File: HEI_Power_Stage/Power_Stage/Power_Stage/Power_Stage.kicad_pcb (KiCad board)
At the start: 6 copper layers, 119.6 x 65.3 mm, 152 parts, among them IC1 ACS730KLCTR-65ABT, IC2 ACS730KLCTR-65ABT, IC3 ACS730KLCTR-65ABT, IC4 AMC1311DWVR, IC9 ACS730KLCTR-65ABT, J1 Screw_Terminal_01x01, J2 Screw_Terminal_01x01, J3 Screw_Terminal_01x01, J4 Screw_Terminal_01x01, J5 Screw_Terminal_01x01, J8 Conn_02x07_Odd_Even, J9 Conn_02x07_Odd_Even, Q1 EPC2304ENGRT, Q2 EPC2304ENGRT, Q3 EPC2304ENGRT, Q4 EPC2304ENGRT, Q5 EPC2304ENGRT, Q6 EPC2304ENGRT, U2 MP18831-4AGY, U3 MP18831-4AGY, U5 MP18831-4AGY

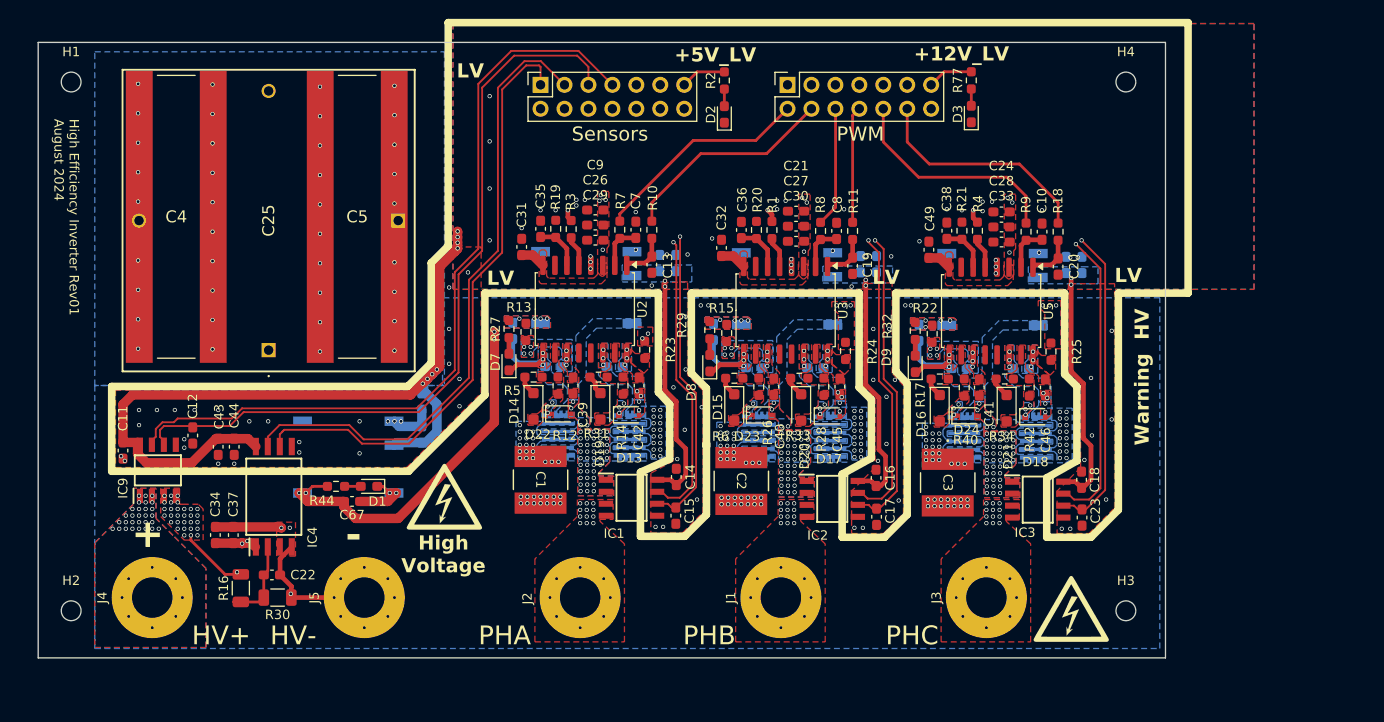
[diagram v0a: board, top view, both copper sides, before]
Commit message: allegro gate driver version schematic overhall and layout
layout and routing almost complete for allegro gate drivers
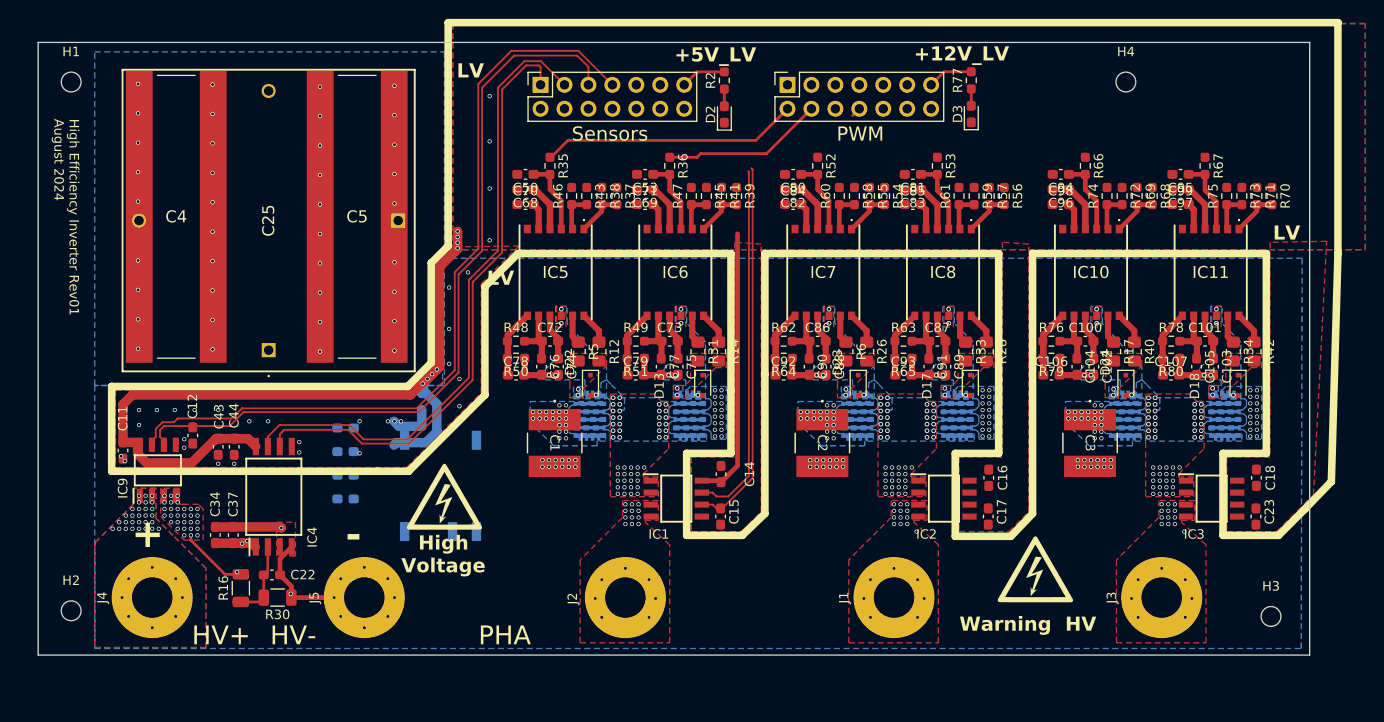
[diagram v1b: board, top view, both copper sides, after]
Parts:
- removed C13, C19, C20: 470pF, Capacitor_SMD:C_0603_1608Metric_Pad1.08x0.95mm_HandSolder
- removed C21, C24: 10uF, Capacitor_SMD:C_0603_1608Metric_Pad1.08x0.95mm_HandSolder
- removed C26, C27, C28, C39, C40, C41, C42, C45, C46, C59, C60, C61, C66: 1uF, Capacitor_SMD:C_0603_1608Metric_Pad1.08x0.95mm_HandSolder
- removed C29, C30, C31, C32, C33, C47, C48, C49, C51, C52, C54, C55: 0.1uF, Capacitor_SMD:C_0603_1608Metric_Pad1.08x0.95mm_HandSolder
- removed C35, C36, C38: 2.2nF, Capacitor_SMD:C_0603_1608Metric_Pad1.08x0.95mm_HandSolder
- removed C56, C57, C58, C62, C63, C64, C65, C67: 4.7uF, Capacitor_SMD:C_0603_1608Metric_Pad1.08x0.95mm_HandSolder
- removed D1, D7, D8, D9: G, LED_SMD:LED_0603_1608Metric_Pad1.05x0.95mm_HandSolder
- removed D14, D15, D16, D19, D20, D21: 300mV 1A, Diode_SMD:D_SOD-123F
- removed PS2, PS3, PS4: CRE1S0505MC, CRE1S0505MC_KiCad:CRE1S0505MC
- removed R1, R10, R11, R13, R15, R18, R22, R23, R24, R25, R3, R4, R7, R8, R9: 0, Resistor_SMD:R_0603_1608Metric_Pad0.98x0.95mm_HandSolder
- removed R19, R20, R21: 10k, Resistor_SMD:R_0603_1608Metric_Pad0.98x0.95mm_HandSolder
- removed R27, R29, R32, R44: 440, Resistor_SMD:R_0603_1608Metric_Pad0.98x0.95mm_HandSolder
- removed U2, U3, U5: MP18831-4AGY, Package_SO:SOIC-16W_7.5x10.3mm_P1.27mm
- added C100: 100nF, Capacitor_SMD:C_0603_1608Metric_Pad1.08x0.95mm_HandSolder, F.Cu at (210.1, 72.7)
- added C101: 100nF, Capacitor_SMD:C_0603_1608Metric_Pad1.08x0.95mm_HandSolder, F.Cu at (222.8, 72.7)
- added C102: 100nF, Capacitor_SMD:C_0603_1608Metric_Pad1.08x0.95mm_HandSolder, F.Cu at (211.0, 75.4)
- added C103: 100nF, Capacitor_SMD:C_0603_1608Metric_Pad1.08x0.95mm_HandSolder, F.Cu at (223.7, 75.4)
- added C104: 100nF, Capacitor_SMD:C_0603_1608Metric_Pad1.08x0.95mm_HandSolder, F.Cu at (209.2, 75.4)
- added C105: 100nF, Capacitor_SMD:C_0603_1608Metric_Pad1.08x0.95mm_HandSolder, F.Cu at (221.9, 75.4)
- added C106: 100pF, Capacitor_SMD:C_0603_1608Metric_Pad1.08x0.95mm_HandSolder, F.Cu at (206.5, 76.3)
- added C107: 100pF, Capacitor_SMD:C_0603_1608Metric_Pad1.08x0.95mm_HandSolder, F.Cu at (219.2, 76.3)
- added C50: 75pF, Capacitor_SMD:C_0603_1608Metric_Pad1.08x0.95mm_HandSolder, F.Cu at (150.7, 55.0)
- added C53: 75pF, Capacitor_SMD:C_0603_1608Metric_Pad1.08x0.95mm_HandSolder, F.Cu at (163.4, 55.0)
- added C68: 1uF, Capacitor_SMD:C_0603_1608Metric_Pad1.08x0.95mm_HandSolder, F.Cu at (150.7, 56.6)
- added C69: 1uF, Capacitor_SMD:C_0603_1608Metric_Pad1.08x0.95mm_HandSolder, F.Cu at (163.4, 56.6)
- added C70: 1uF, Capacitor_SMD:C_0603_1608Metric_Pad1.08x0.95mm_HandSolder, F.Cu at (150.7, 58.2)
- added C71: 1uF, Capacitor_SMD:C_0603_1608Metric_Pad1.08x0.95mm_HandSolder, F.Cu at (163.4, 58.2)
- added C72: 100nF, Capacitor_SMD:C_0603_1608Metric_Pad1.08x0.95mm_HandSolder, F.Cu at (153.3, 72.7)
- added C73: 100nF, Capacitor_SMD:C_0603_1608Metric_Pad1.08x0.95mm_HandSolder, F.Cu at (166.0, 72.7)
- added C74: 100nF, Capacitor_SMD:C_0603_1608Metric_Pad1.08x0.95mm_HandSolder, F.Cu at (154.2, 75.4)
- added C75: 100nF, Capacitor_SMD:C_0603_1608Metric_Pad1.08x0.95mm_HandSolder, F.Cu at (166.9, 75.4)
- added C76: 100nF, Capacitor_SMD:C_0603_1608Metric_Pad1.08x0.95mm_HandSolder, F.Cu at (152.4, 75.4)
- added C77: 100nF, Capacitor_SMD:C_0603_1608Metric_Pad1.08x0.95mm_HandSolder, F.Cu at (165.1, 75.4)
- added C78: 100pF, Capacitor_SMD:C_0603_1608Metric_Pad1.08x0.95mm_HandSolder, F.Cu at (149.7, 76.3)
- added C79: 100pF, Capacitor_SMD:C_0603_1608Metric_Pad1.08x0.95mm_HandSolder, F.Cu at (162.4, 76.3)
- added C80: 75pF, Capacitor_SMD:C_0603_1608Metric_Pad1.08x0.95mm_HandSolder, F.Cu at (179.1, 55.0)
- added C81: 75pF, Capacitor_SMD:C_0603_1608Metric_Pad1.08x0.95mm_HandSolder, F.Cu at (191.8, 55.0)
- added C82: 1uF, Capacitor_SMD:C_0603_1608Metric_Pad1.08x0.95mm_HandSolder, F.Cu at (179.1, 56.6)
- added C83: 1uF, Capacitor_SMD:C_0603_1608Metric_Pad1.08x0.95mm_HandSolder, F.Cu at (191.8, 56.6)
- added C84: 1uF, Capacitor_SMD:C_0603_1608Metric_Pad1.08x0.95mm_HandSolder, F.Cu at (179.1, 58.2)
- added C85: 1uF, Capacitor_SMD:C_0603_1608Metric_Pad1.08x0.95mm_HandSolder, F.Cu at (191.8, 58.2)
- added C86: 100nF, Capacitor_SMD:C_0603_1608Metric_Pad1.08x0.95mm_HandSolder, F.Cu at (181.7, 72.7)
- added C87: 100nF, Capacitor_SMD:C_0603_1608Metric_Pad1.08x0.95mm_HandSolder, F.Cu at (194.4, 72.7)
- added C88: 100nF, Capacitor_SMD:C_0603_1608Metric_Pad1.08x0.95mm_HandSolder, F.Cu at (182.6, 75.4)
- added C89: 100nF, Capacitor_SMD:C_0603_1608Metric_Pad1.08x0.95mm_HandSolder, F.Cu at (195.3, 75.4)
- added C90: 100nF, Capacitor_SMD:C_0603_1608Metric_Pad1.08x0.95mm_HandSolder, F.Cu at (180.8, 75.4)
- added C91: 100nF, Capacitor_SMD:C_0603_1608Metric_Pad1.08x0.95mm_HandSolder, F.Cu at (193.5, 75.4)
- added C92: 100pF, Capacitor_SMD:C_0603_1608Metric_Pad1.08x0.95mm_HandSolder, F.Cu at (178.1, 76.3)
- added C93: 100pF, Capacitor_SMD:C_0603_1608Metric_Pad1.08x0.95mm_HandSolder, F.Cu at (190.8, 76.3)
- added C94: 75pF, Capacitor_SMD:C_0603_1608Metric_Pad1.08x0.95mm_HandSolder, F.Cu at (207.5, 55.0)
- added C95: 75pF, Capacitor_SMD:C_0603_1608Metric_Pad1.08x0.95mm_HandSolder, F.Cu at (220.2, 55.0)
- added C96: 1uF, Capacitor_SMD:C_0603_1608Metric_Pad1.08x0.95mm_HandSolder, F.Cu at (207.5, 56.6)
- added C97: 1uF, Capacitor_SMD:C_0603_1608Metric_Pad1.08x0.95mm_HandSolder, F.Cu at (220.2, 56.6)
- added C98: 1uF, Capacitor_SMD:C_0603_1608Metric_Pad1.08x0.95mm_HandSolder, F.Cu at (207.5, 58.2)
- added C99: 1uF, Capacitor_SMD:C_0603_1608Metric_Pad1.08x0.95mm_HandSolder, F.Cu at (220.2, 58.2)
- added IC10: AHV85111KNHTR, AHV85111_KiCad:AHV85111KNHTR, F.Cu at (210.7, 65.4)
- added IC11: AHV85111KNHTR, AHV85111_KiCad:AHV85111KNHTR, F.Cu at (223.4, 65.4)
- added IC5: AHV85111KNHTR, AHV85111_KiCad:AHV85111KNHTR, F.Cu at (153.9, 65.4)
- added IC6: AHV85111KNHTR, AHV85111_KiCad:AHV85111KNHTR, F.Cu at (166.6, 65.4)
- added IC7: AHV85111KNHTR, AHV85111_KiCad:AHV85111KNHTR, F.Cu at (182.3, 65.4)
- added IC8: AHV85111KNHTR, AHV85111_KiCad:AHV85111KNHTR, F.Cu at (195.0, 65.4)
- added R35: 0, Resistor_SMD:R_0603_1608Metric_Pad0.98x0.95mm_HandSolder, F.Cu at (153.3, 54.1)
- added R36: 0, Resistor_SMD:R_0603_1608Metric_Pad0.98x0.95mm_HandSolder, F.Cu at (166.0, 54.1)
- added R37: 0, Resistor_SMD:R_0603_1608Metric_Pad0.98x0.95mm_HandSolder, F.Cu at (160.4, 57.3)
- added R38: 0, Resistor_SMD:R_0603_1608Metric_Pad0.98x0.95mm_HandSolder, F.Cu at (158.8, 57.3)
- added R39: 0, Resistor_SMD:R_0603_1608Metric_Pad0.98x0.95mm_HandSolder, F.Cu at (173.1, 57.3)
- added R41: 0, Resistor_SMD:R_0603_1608Metric_Pad0.98x0.95mm_HandSolder, F.Cu at (171.5, 57.3)
- added R43: 100k, Resistor_SMD:R_0603_1608Metric_Pad0.98x0.95mm_HandSolder, F.Cu at (157.2, 57.3)
- added R45: 100k, Resistor_SMD:R_0603_1608Metric_Pad0.98x0.95mm_HandSolder, F.Cu at (169.9, 57.3)
- added R46: 0, Resistor_SMD:R_0603_1608Metric_Pad0.98x0.95mm_HandSolder, F.Cu at (155.6, 57.3)
- added R47: 0, Resistor_SMD:R_0603_1608Metric_Pad0.98x0.95mm_HandSolder, F.Cu at (168.3, 57.3)
- added R48: 32.4k, Resistor_SMD:R_0603_1608Metric_Pad0.98x0.95mm_HandSolder, F.Cu at (149.7, 72.7)
- added R49: 32.4k, Resistor_SMD:R_0603_1608Metric_Pad0.98x0.95mm_HandSolder, F.Cu at (162.4, 72.7)
- added R50: 100k, Resistor_SMD:R_0603_1608Metric_Pad0.98x0.95mm_HandSolder, F.Cu at (149.7, 74.5)
- added R51: 100k, Resistor_SMD:R_0603_1608Metric_Pad0.98x0.95mm_HandSolder, F.Cu at (162.4, 74.5)
- added R52: 0, Resistor_SMD:R_0603_1608Metric_Pad0.98x0.95mm_HandSolder, F.Cu at (181.7, 54.1)
- added R53: 0, Resistor_SMD:R_0603_1608Metric_Pad0.98x0.95mm_HandSolder, F.Cu at (194.4, 54.1)
- added R54: 0, Resistor_SMD:R_0603_1608Metric_Pad0.98x0.95mm_HandSolder, F.Cu at (188.8, 57.3)
- added R55: 0, Resistor_SMD:R_0603_1608Metric_Pad0.98x0.95mm_HandSolder, F.Cu at (187.2, 57.3)
- added R56: 0, Resistor_SMD:R_0603_1608Metric_Pad0.98x0.95mm_HandSolder, F.Cu at (201.5, 57.3)
- added R57: 0, Resistor_SMD:R_0603_1608Metric_Pad0.98x0.95mm_HandSolder, F.Cu at (199.9, 57.3)
- added R58: 100k, Resistor_SMD:R_0603_1608Metric_Pad0.98x0.95mm_HandSolder, F.Cu at (185.6, 57.3)
- added R59: 100k, Resistor_SMD:R_0603_1608Metric_Pad0.98x0.95mm_HandSolder, F.Cu at (198.3, 57.3)
- added R60: 0, Resistor_SMD:R_0603_1608Metric_Pad0.98x0.95mm_HandSolder, F.Cu at (184.0, 57.3)
- added R61: 0, Resistor_SMD:R_0603_1608Metric_Pad0.98x0.95mm_HandSolder, F.Cu at (196.7, 57.3)
- added R62: 32.4k, Resistor_SMD:R_0603_1608Metric_Pad0.98x0.95mm_HandSolder, F.Cu at (178.1, 72.7)
- added R63: 32.4k, Resistor_SMD:R_0603_1608Metric_Pad0.98x0.95mm_HandSolder, F.Cu at (190.8, 72.7)
- added R64: 100k, Resistor_SMD:R_0603_1608Metric_Pad0.98x0.95mm_HandSolder, F.Cu at (178.1, 74.5)
- added R65: 100k, Resistor_SMD:R_0603_1608Metric_Pad0.98x0.95mm_HandSolder, F.Cu at (190.8, 74.5)
- added R66: 0, Resistor_SMD:R_0603_1608Metric_Pad0.98x0.95mm_HandSolder, F.Cu at (210.1, 54.1)
- added R67: 0, Resistor_SMD:R_0603_1608Metric_Pad0.98x0.95mm_HandSolder, F.Cu at (222.8, 54.1)
- added R68: 0, Resistor_SMD:R_0603_1608Metric_Pad0.98x0.95mm_HandSolder, F.Cu at (217.2, 57.3)
- added R69: 0, Resistor_SMD:R_0603_1608Metric_Pad0.98x0.95mm_HandSolder, F.Cu at (215.6, 57.3)
- added R70: 0, Resistor_SMD:R_0603_1608Metric_Pad0.98x0.95mm_HandSolder, F.Cu at (229.9, 57.3)
- added R71: 0, Resistor_SMD:R_0603_1608Metric_Pad0.98x0.95mm_HandSolder, F.Cu at (228.3, 57.3)
- added R72: 100k, Resistor_SMD:R_0603_1608Metric_Pad0.98x0.95mm_HandSolder, F.Cu at (214.0, 57.3)
- added R73: 100k, Resistor_SMD:R_0603_1608Metric_Pad0.98x0.95mm_HandSolder, F.Cu at (226.7, 57.3)
- added R74: 0, Resistor_SMD:R_0603_1608Metric_Pad0.98x0.95mm_HandSolder, F.Cu at (212.4, 57.3)
- added R75: 0, Resistor_SMD:R_0603_1608Metric_Pad0.98x0.95mm_HandSolder, F.Cu at (225.1, 57.3)
- added R76: 32.4k, Resistor_SMD:R_0603_1608Metric_Pad0.98x0.95mm_HandSolder, F.Cu at (206.5, 72.7)
- added R78: 32.4k, Resistor_SMD:R_0603_1608Metric_Pad0.98x0.95mm_HandSolder, F.Cu at (219.2, 72.7)
- added R79: 100k, Resistor_SMD:R_0603_1608Metric_Pad0.98x0.95mm_HandSolder, F.Cu at (206.5, 74.5)
- added R80: 100k, Resistor_SMD:R_0603_1608Metric_Pad0.98x0.95mm_HandSolder, F.Cu at (219.2, 74.5)
- C10, C8: value 470pF -> 2.2uF; moved to B.Cu
- C7: value 470pF -> 1uF; moved to B.Cu
- C9: value 10uF -> 1uF; moved to B.Cu
- R12, R14, R26, R28, R40, R42: footprint Resistor_SMD:R_0603_1608Metric_Pad0.98x0.95mm_HandSolder -> Resistor_SMD:R_0805_2012Metric_Pad1.20x1.40mm_HandSolder
- R17, R31, R33, R34, R5, R6: value 0 -> 0.5; footprint Resistor_SMD:R_0603_1608Metric_Pad0.98x0.95mm_HandSolder -> Resistor_SMD:R_0805_2012Metric_Pad1.20x1.40mm_HandSolder
- moved C10 79.1 mm to (131.6, 89.4), turned to 180 degrees
- moved C8 57.1 mm to (131.6, 84.4), turned to 180 degrees
- moved C9 38.7 mm to (131.6, 86.9), turned to 180 degrees
- moved C7 37.3 mm to (131.6, 81.9), turned to 180 degrees
- moved PS1 26.1 mm to (141.7, 88.0), turned to 180 degrees
- moved R34 24.4 mm to (225.8, 73.8), turned to -90 degrees
- moved R42 24.2 mm to (228.0, 73.8)
- moved D18 21.8 mm to (226.3, 77.4), turned to -90 degrees
- moved Q6 20.2 mm to (224.9, 80.6)
- moved R17 18.7 mm to (213.1, 73.8), turned to -90 degrees
- moved J3 18.6 mm to (218.2, 99.9)
- moved C18 18.6 mm to (228.2, 87.2)
- moved C23 18.5 mm to (228.2, 91.3)
- moved IC3 18.5 mm to (223.5, 89.4)
- moved R40 18.4 mm to (215.3, 73.8)
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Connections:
- C10 pad 2: /Phase3/INB -> +5V_LV
- C7 pad 1: GND -> HV-
- C7 pad 2: /Phase1/INB -> +5V_HV
- C8 pad 1: GND -> HV-
- C8 pad 2: /Phase2/INB -> +5V_HV
- PS1 pad 7: /Phase1/SW -> HV-
- PS1 pad 8: /Phase1/VDDA -> +5V_HV
- R12 pad 1: /Phase1/HS_{DRV} -> /Phase1/HS_{SRC}
- R14 pad 1: /Phase1/LS_{DRV} -> /Phase1/LS_{SRC}
- R17 pad 1: /Phase3/HS_{DRV} -> /Phase3/HS_{SNK}
- R17 pad 2: Net-(D16-K) -> /Phase3/HS_{Gate}
- R26 pad 1: /Phase2/HS_{DRV} -> /Phase2/HS_{SRC}
- R28 pad 1: /Phase2/LS_{DRV} -> /Phase2/LS_{SRC}
- R31 pad 1: /Phase1/LS_{DRV} -> /Phase1/LS_{SNK}
- R31 pad 2: Net-(D19-K) -> /Phase1/LS_{Gate}
- R33 pad 1: /Phase2/LS_{DRV} -> /Phase2/LS_{SNK}
- R33 pad 2: Net-(D20-K) -> /Phase2/LS_{Gate}
- R34 pad 1: /Phase3/LS_{DRV} -> /Phase3/LS_{SNK}
- R34 pad 2: Net-(D21-K) -> /Phase3/LS_{Gate}
- R40 pad 1: /Phase3/HS_{DRV} -> /Phase3/HS_{SRC}
- R42 pad 1: /Phase3/LS_{DRV} -> /Phase3/LS_{SRC}
- R5 pad 1: /Phase1/HS_{DRV} -> /Phase1/HS_{SNK}
- R5 pad 2: Net-(D14-K) -> /Phase1/HS_{Gate}
- R6 pad 1: /Phase2/HS_{DRV} -> /Phase2/HS_{SNK}
- R6 pad 2: Net-(D15-K) -> /Phase2/HS_{Gate}
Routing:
- net +5V_HV: track 117.4 -> 12.1 mm, vias 18 -> 2
- net +5V_LV: track 178.5 -> 118.7 mm, vias 27 -> 8
- net /PHCI_{sense}-: track 86.5 -> 53.5 mm, vias 1 -> 0
- net /PHBI_{sense}-: track 67.6 -> 35.0 mm, vias 1 -> 0
- net /PHBI_{sense}+: track 67.6 -> 35.9 mm, vias 1 -> 0
- net /PHCI_{sense}+: track 85.5 -> 53.8 mm, vias 1 -> 0
- net +12V_LV: track 4.83 -> 34.8 mm
- net /CLS_{PWM}: track 24.4 -> 0.00 mm
- net /CHS_{PWM}: track 23.9 -> 0.00 mm
- net /BHS_{PWM}: track 12.7 -> 0.03 mm
- net HV-: track 28.0 -> 40.4 mm, vias 143 -> 128
- net /BLS_{PWM}: track 12.3 -> 1.01 mm
- net /Phase1/lpwm: track 0.00 -> 8.03 mm
- net /Phase3/lpwm: track 0.00 -> 8.03 mm
- net /Phase3/hpwm: track 0.00 -> 8.03 mm
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- added copper zone on In3.Cu, net +12V_LV
- added copper zone on In1.Cu, net /Phase1/SW
- added copper zone on In1.Cu, net /Phase2/SW
- added copper zone on In1.Cu, net /Phase3/SW
- removed copper zone on F.Cu, net +5V_HV
- removed copper zone on B.Cu, net +5V_LV
- removed copper zone on F.Cu, net +5V_LV
- removed copper zone on F.Cu, net /Phase1/HS_{DRV}
- removed copper zone on F.Cu, net /Phase1/LS_{DRV}
- removed copper zone on In4.Cu, net /Phase1/SW
- removed copper zone on B.Cu, net /Phase1/VDDA
- removed copper zone on F.Cu, net /Phase1/VDDA
- removed copper zone on B.Cu, net /Phase1/VDDhs
- removed copper zone on F.Cu, net /Phase1/VDDhs
- removed copper zone on B.Cu, net /Phase1/VDDls
- removed copper zone on F.Cu, net /Phase1/VDDls
- removed copper zone on F.Cu, net /Phase2/HS_{DRV}
- removed copper zone on F.Cu, net /Phase2/LS_{DRV}
- removed copper zone on In4.Cu, net /Phase2/SW
- removed copper zone on B.Cu, net /Phase2/VDDA
- removed copper zone on F.Cu, net /Phase2/VDDA
- removed copper zone on B.Cu, net /Phase2/VDDhs
- removed copper zone on F.Cu, net /Phase2/VDDhs
- removed copper zone on B.Cu, net /Phase2/VDDls
- removed copper zone on F.Cu, net /Phase2/VDDls
- removed copper zone on F.Cu, net /Phase3/HS_{DRV}
- removed copper zone on F.Cu, net /Phase3/LS_{DRV}
- removed copper zone on In4.Cu, net /Phase3/SW
- removed copper zone on B.Cu, net /Phase3/VDDA
- removed copper zone on F.Cu, net /Phase3/VDDA
- removed copper zone on B.Cu, net /Phase3/VDDhs
- removed copper zone on F.Cu, net /Phase3/VDDhs
- removed copper zone on B.Cu, net /Phase3/VDDls
- removed copper zone on F.Cu, net /Phase3/VDDls
- removed copper zone on In3.Cu, net GND
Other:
- board size 119.6 x 65.3 mm -> 134.9 x 65 mm
- board text removed: "PHB"
- board text removed: "PHC"

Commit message: allegro power stage routed
needs drc check and silkscreen for all components
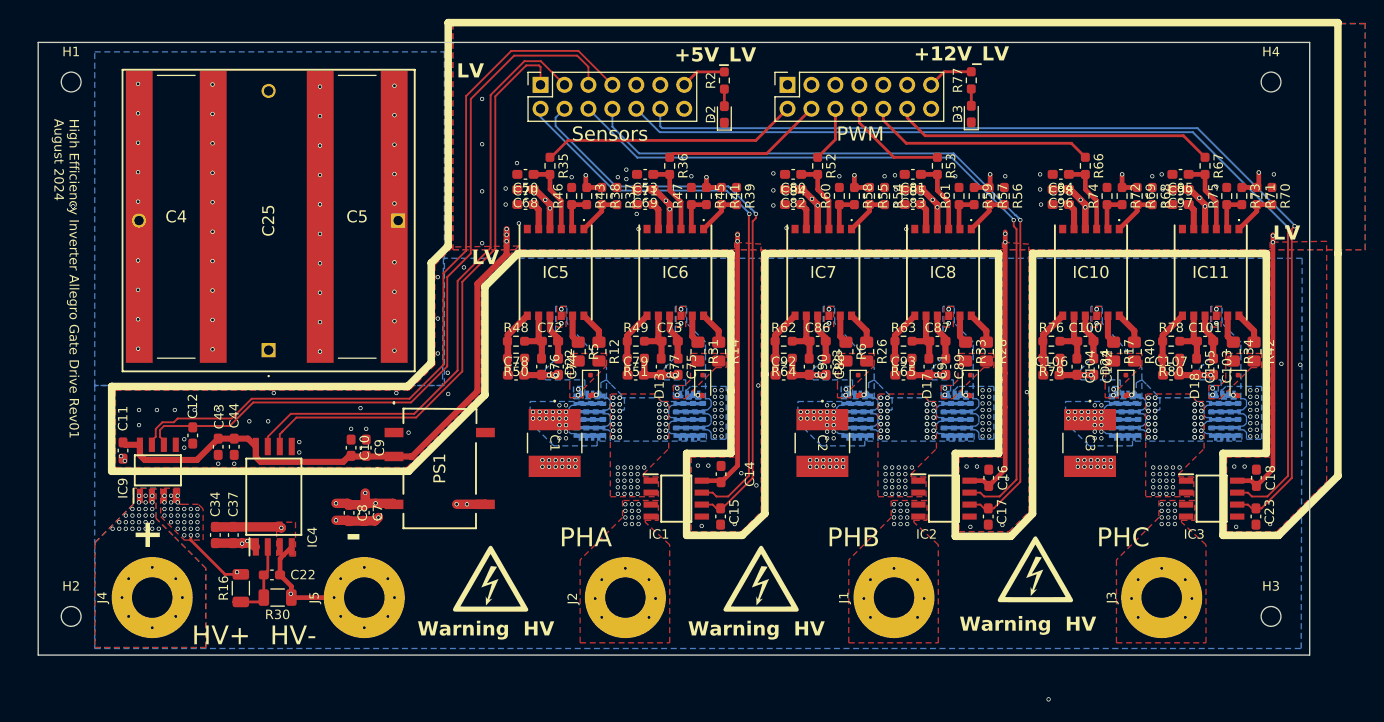
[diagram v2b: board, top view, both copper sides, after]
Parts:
- added G***: LOGO, LOGO, F.Cu at (175.7, 97.9)
- C10, C7, C8, C9, PS1: moved to F.Cu
- moved H4 15.4 mm to (229.8, 45.2)
- moved G*** 9.98 mm to (147.0, 97.9)
- moved C7 9.21 mm to (133.6, 90.9), turned to -90 degrees
- moved C8 6.51 mm to (132.0, 90.9), turned to -90 degrees
- moved C10 5.47 mm to (132.2, 84.0), turned to -90 degrees
- moved C9 3.65 mm to (133.8, 84.0), turned to -90 degrees
- moved PS1 1.85 mm to (141.6, 86.2), turned to -90 degrees
- moved H2 0.60 mm to (102.5, 101.9)
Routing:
- net /PHCI_{sense}-: track 53.5 -> 107.7 mm, vias 0 -> 1
- net /PHCI_{sense}+: track 53.8 -> 107.2 mm, vias 0 -> 1
- net /PHBI_{sense}-: track 35.0 -> 83.8 mm, vias 0 -> 1
- net /PHBI_{sense}+: track 35.9 -> 83.6 mm, vias 0 -> 1
- net +5V_LV: track 118.7 -> 157.1 mm, vias 8 -> 9
- net /CLS_{PWM}: track 0.00 -> 34.3 mm
- net +5V_HV: track 12.1 -> 37.9 mm, vias 2 -> 6
- net /CHS_{PWM}: track 0.00 -> 24.3 mm
- net +12V_LV: track 34.8 -> 52.7 mm, vias 0 -> 18
- net /BLS_{PWM}: track 1.01 -> 11.3 mm
- net HV-: track 40.4 -> 48.0 mm, vias 128 -> 131
- net /BHS_{PWM}: track 0.03 -> 5.95 mm
- net GND: track 4.95 -> 0.00 mm, vias 31 -> 86
- net /DCV_{sense}+: track 66.8 -> 64.4 mm
- net /DCV_{sense}-: track 63.9 -> 61.5 mm
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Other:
- board text added: "High Efficiency Inverter Allegro Gate Drive Rev01 August 2024"
- board text added: "PHB"
- board text added: "PHC"
- board text removed: "High Efficiency Inverter Rev01 August 2024"
- board text removed: "High Voltage"

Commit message: done
silkscreen done and bom done in digikey
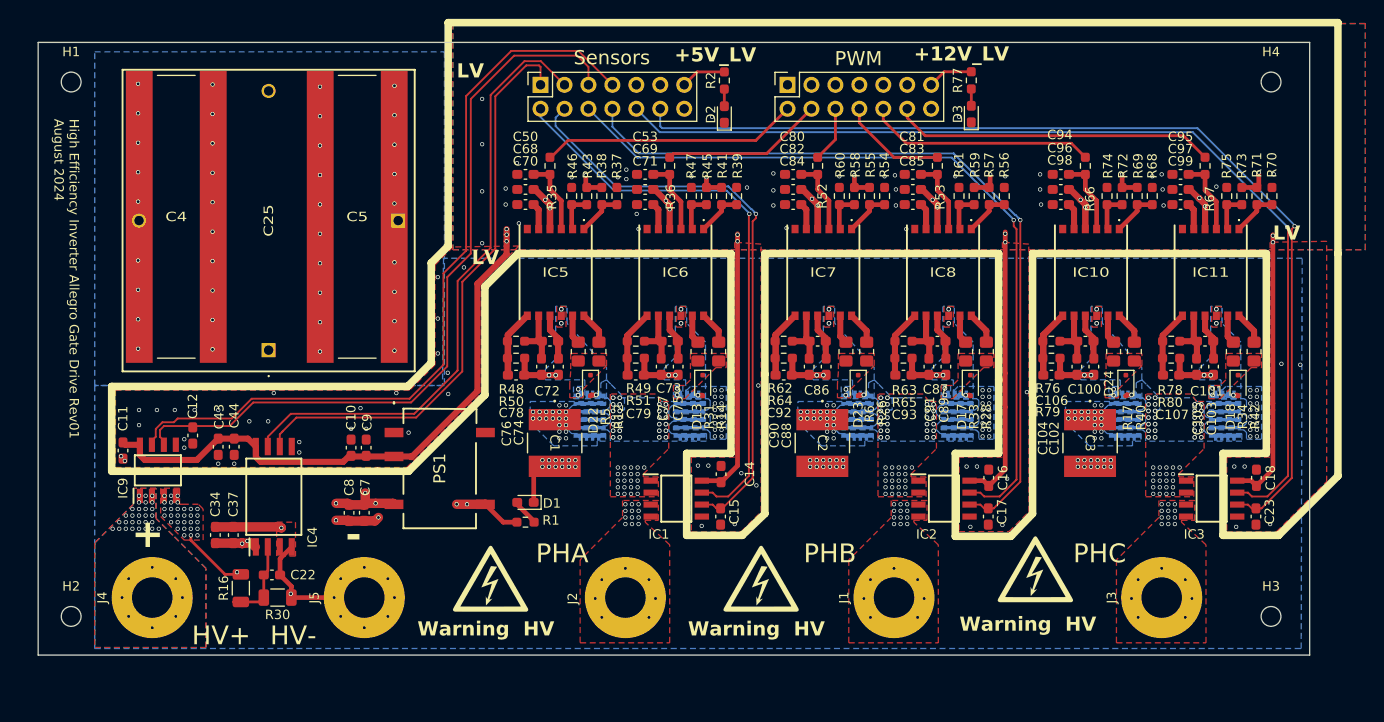
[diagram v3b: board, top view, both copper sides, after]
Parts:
- added D1: G, LED_SMD:LED_0603_1608Metric_Pad1.05x0.95mm_HandSolder, F.Cu at (150.7, 89.8)
- added G***: LOGO, LOGO, B.Cu at (175.6, 70.0)
- added G***: LOGO, LOGO, B.Cu at (203.2, 69.9)
- added G***: LOGO, LOGO, B.Cu at (121.1, 89.2)
- added R1: 440, Resistor_SMD:R_0603_1608Metric_Pad0.98x0.95mm_HandSolder, F.Cu at (150.7, 91.9)
- C11, C14, C16, C18: value 0.1uF -> 100nF
- C50, C53, C80, C81, C94, C95: value 75pF -> 100pF
- R12, R14, R26, R28, R40, R42: value 0.75 -> 0.47
- R17, R31, R33, R34, R5, R6: value 0.5 -> 0
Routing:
- net HV-: track 48.0 -> 52.1 mm
- net +5V_HV: track 37.9 -> 42.1 mm
- net Net-(D1-A): track 0.00 -> 2.84 mm
- net (no net): vias 3 -> 0

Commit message: some changes
isolated amplifier now self powered so removed old amp and iso power supply
gate return paths now on layer two
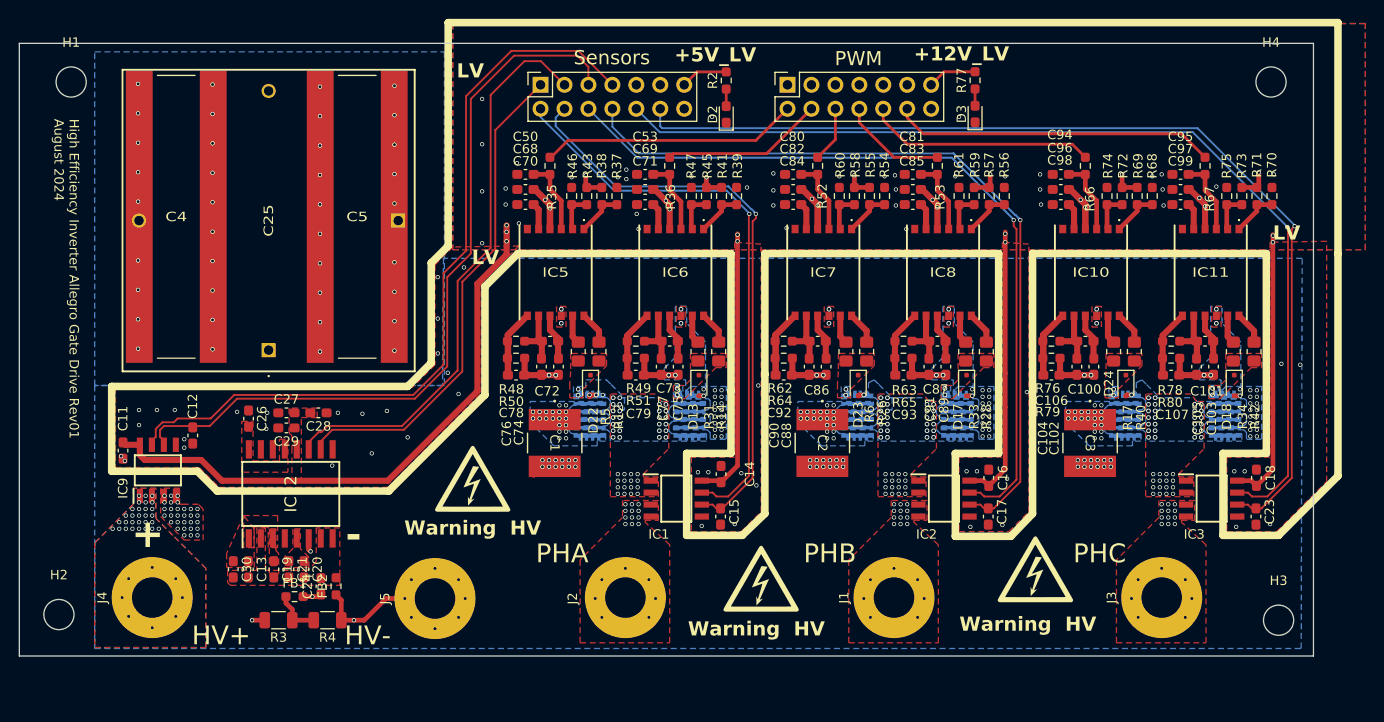
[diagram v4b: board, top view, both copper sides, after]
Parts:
- removed C10, C8: 2.2uF, Capacitor_SMD:C_0603_1608Metric_Pad1.08x0.95mm_HandSolder
- removed C22: 10nF, Capacitor_SMD:C_0603_1608Metric_Pad1.08x0.95mm_HandSolder
- removed C34, C43, C7, C9: 1uF, Capacitor_SMD:C_0603_1608Metric_Pad1.08x0.95mm_HandSolder
- removed C37, C44: 100nF, Capacitor_SMD:C_0603_1608Metric_Pad1.08x0.95mm_HandSolder
- removed D1: G, LED_SMD:LED_0603_1608Metric_Pad1.05x0.95mm_HandSolder
- removed IC4: AMC1311DWVR, AMC1311_KiCad:SOIC127P1150X280-8N
- removed PS1: CRE1S0505MC, CRE1S0505MC_KiCad:CRE1S0505MC
- removed R1: 440, Resistor_SMD:R_0603_1608Metric_Pad0.98x0.95mm_HandSolder
- removed R16: 1Meg, Resistor_SMD:R_1206_3216Metric
- removed R30: 10k, Resistor_SMD:R_1206_3216Metric
- added C13: 1nF, Capacitor_SMD:C_0603_1608Metric_Pad1.08x0.95mm_HandSolder, F.Cu at (121.3, 96.9)
- added C19: 100nF, Capacitor_SMD:C_0603_1608Metric_Pad1.08x0.95mm_HandSolder, F.Cu at (124.0, 96.9)
- added C20: 100nF, Capacitor_SMD:C_0603_1608Metric_Pad1.08x0.95mm_HandSolder, F.Cu at (127.2, 96.9)
- added C21: 1nF, Capacitor_SMD:C_0603_1608Metric_Pad1.08x0.95mm_HandSolder, F.Cu at (125.6, 96.9)
- added C24: 100pF, Capacitor_SMD:C_0603_1608Metric_Pad1.08x0.95mm_HandSolder, F.Cu at (129.0, 98.7)
- added C26: 100nF, Capacitor_SMD:C_0603_1608Metric_Pad1.08x0.95mm_HandSolder, F.Cu at (121.3, 80.9)
- added C27: 1uF, Capacitor_SMD:C_0603_1608Metric_Pad1.08x0.95mm_HandSolder, F.Cu at (125.3, 80.3)
- added C28: 2.2uF, Capacitor_SMD:C_0603_1608Metric_Pad1.08x0.95mm_HandSolder, F.Cu at (128.7, 80.3)
- added C29: 1nF, Capacitor_SMD:C_0603_1608Metric_Pad1.08x0.95mm_HandSolder, F.Cu at (125.3, 81.9)
- added C30: 1uF, Capacitor_SMD:C_0603_1608Metric_Pad1.08x0.95mm_HandSolder, F.Cu at (119.7, 96.9)
- added FB1: ~, Resistor_SMD:R_0603_1608Metric_Pad0.98x0.95mm_HandSolder, F.Cu at (126.2, 99.8)
- added FB2: ~, Resistor_SMD:R_0603_1608Metric_Pad0.98x0.95mm_HandSolder, F.Cu at (130.6, 98.7)
- added IC12: AMC3311QDWERQ1, AMC3311_KiCad:SOIC127P1030X265-16N, F.Cu at (125.8, 88.9)
- added R3: 1Meg, Resistor_SMD:R_1206_3216Metric, F.Cu at (124.5, 102.3)
- added R4: 10k, Resistor_SMD:R_1206_3216Metric, F.Cu at (129.7, 102.3)
- H1, H2, H3, H4: footprint MountingHole:MountingHole_2.1mm -> MountingHole:MountingHole_3.2mm_M3
- moved G*** 10.8 mm to (145.1, 87.3)
- moved J5 7.50 mm to (141.1, 100.0)
- moved H2 1.32 mm to (101.2, 101.7)
- moved H3 0.89 mm to (230.6, 102.3)
- moved D17 0.40 mm to (197.5, 77.4)
- moved D13 0.40 mm to (169.1, 77.4)
- moved D18 0.40 mm to (225.9, 77.4)
- moved D3 0.40 mm to (198.4, 48.6)
- moved R77 0.40 mm to (198.4, 45.0)
- moved D2 0.20 mm to (172.0, 48.6)
- moved R2 0.20 mm to (172.0, 45.0)
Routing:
- net +5V_HV: track 42.1 -> 0.00 mm, vias 6 -> 0
- net HV-: track 52.1 -> 30.9 mm, vias 131 -> 130
- net Net-(IC4-VIN): track 9.78 -> 0.00 mm
- net /DCV_{sense}-: track 61.5 -> 52.8 mm
- net /vsnsin: track 0.00 -> 8.33 mm, vias 0 -> 2
- net HV+: track 6.51 -> 1.34 mm
- net Net-(FB1-Pad1): track 0.00 -> 5.05 mm
- net /DCV_{sense}+: track 64.4 -> 60.8 mm
- net Net-(D1-A): track 2.84 -> 0.00 mm
- net +5V_LV: track 157.1 -> 156.4 mm
- net /Phase1/SW: track 6.12 -> 6.52 mm, vias 52 -> 49
- net GND: vias 86 -> 81
- net /Phase3/SW: vias 52 -> 47
- net /Phase2/SW: vias 52 -> 47
- added copper zone on F.Cu, net +5V_LV
- added copper zone on F.Cu, net /dcdc_out
- added copper zone on F.Cu, net /hgnd
- added copper zone on F.Cu, net /hldo_out
- added copper zone on In1.Cu, net HV-
- added copper zone on F.Cu, net Net-(IC12-DCDC_IN)
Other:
- board size 134.9 x 65 mm -> 137.3 x 65 mm
